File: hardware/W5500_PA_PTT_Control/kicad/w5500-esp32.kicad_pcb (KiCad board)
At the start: 2 copper layers, 115 x 72 mm, 19 parts, among them J1 ESP32_DevKitC_Socket_40P_25.4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, Q1 2SC1815, Q3 2SC1815, Q5 2SJ334, U1 TA48033S, U2 L7805

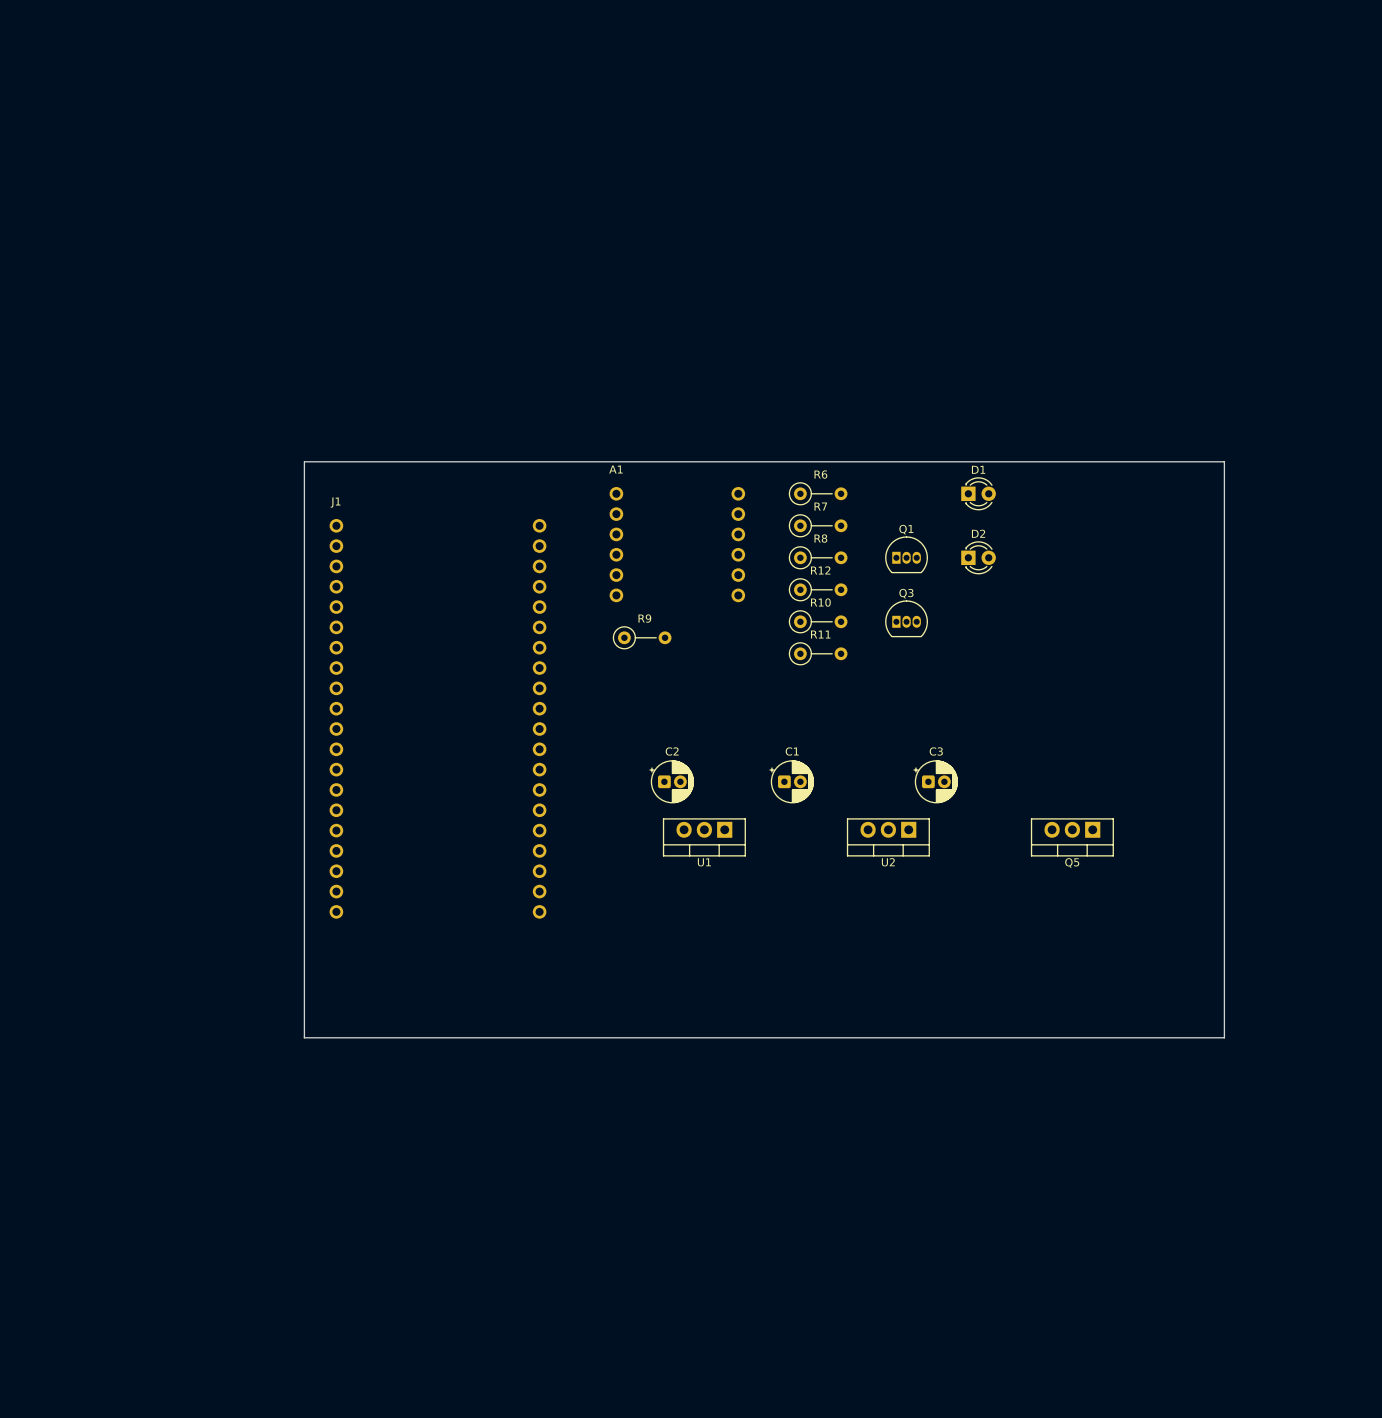
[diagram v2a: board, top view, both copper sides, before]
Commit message: W5500制御基板を縦72×115mmにし、従来基板と同じくW5500を上・ESP32を下に配置
- 外形を横72mm×縦115mm(従来の手配線基板95×72mmを縦に20mm延長)に変更
- 左上にW5500モジュール(RJ45は上端側)、その下にJ1(ESP32 DevKitC、USBは下端側)、
  右側にTO-220(U1・U2・Q5)を縦に23mm間隔で並べ放熱器を右端側に、右下に小物部品とJ2/J5/J6の場所
- W5500モジュール・DevKitC・放熱器・J2/J5/J6の範囲をDwgs.Userに記入(寸法は実物のデータで更新予定)
- DRC違反0件(未配線・J2/J5/J6未指定・既存のGND<NO NET>を除く)。仕様書の配置説明を更新

Co-Authored-By: Claude Opus 5.5 <noreply@anthropic.com>
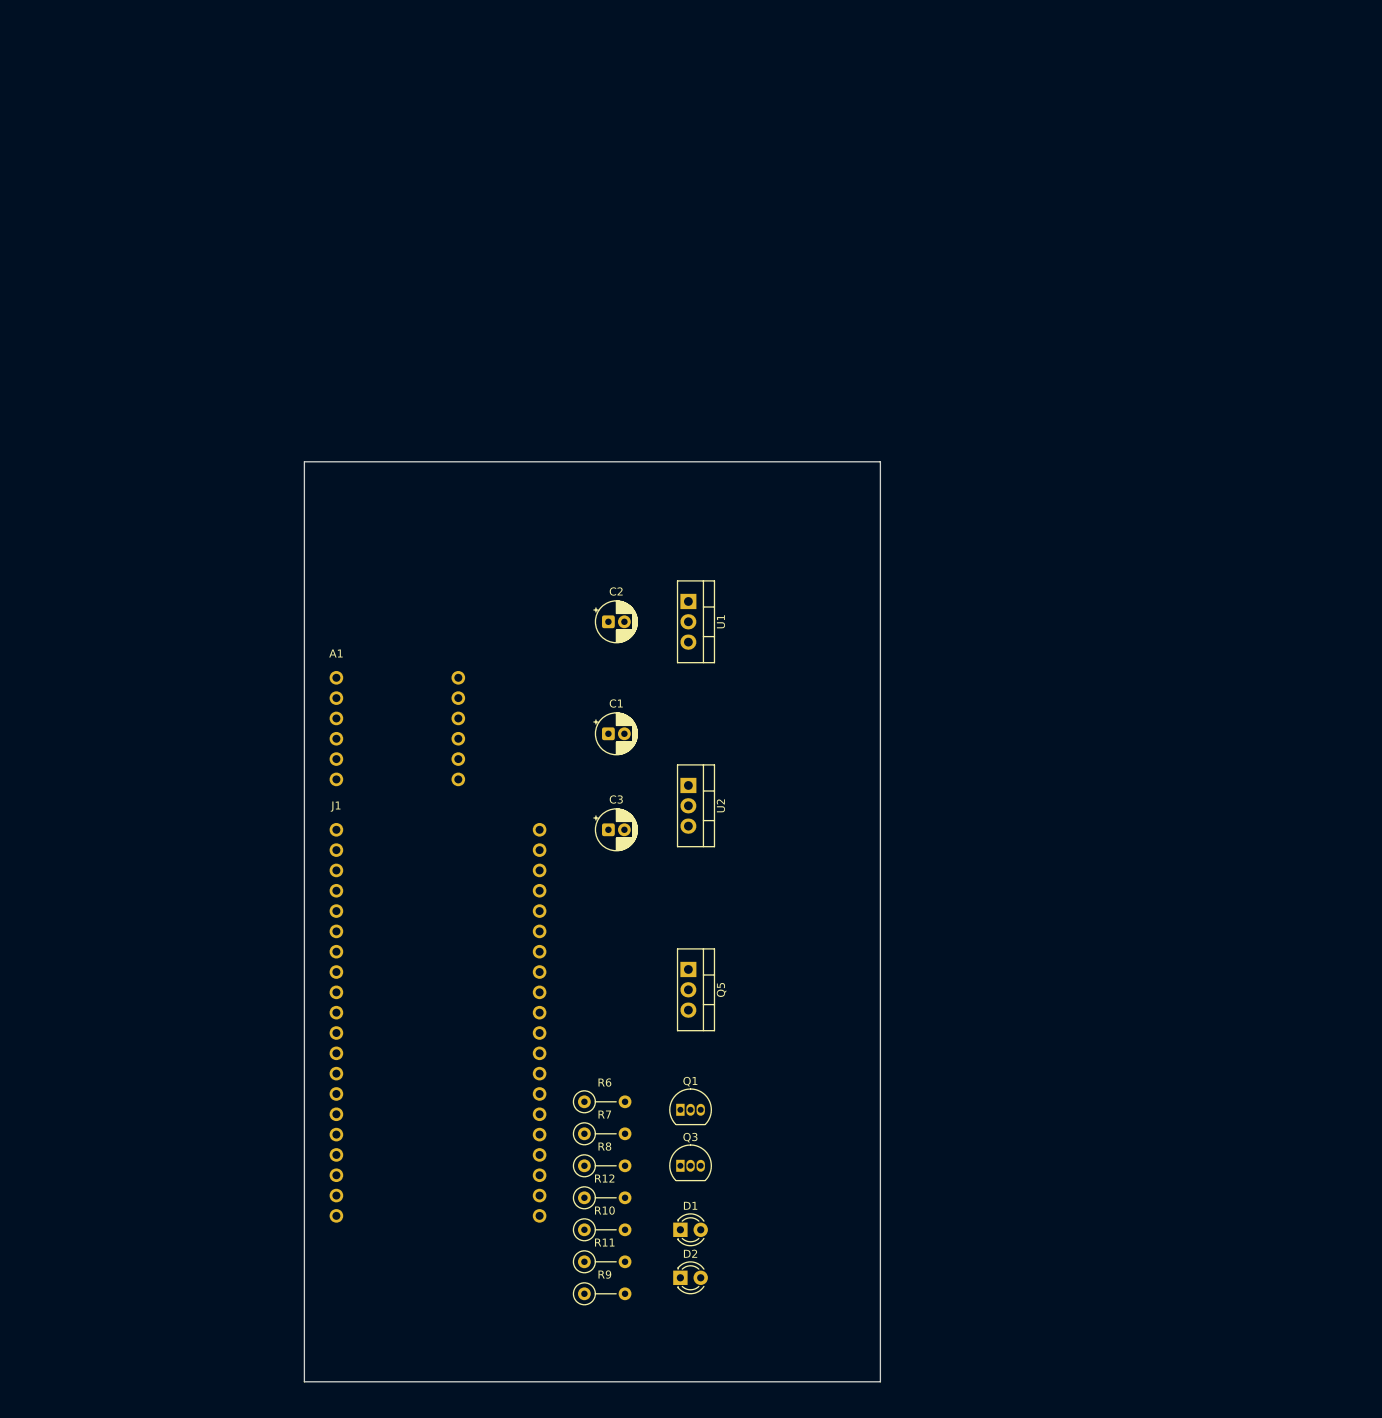
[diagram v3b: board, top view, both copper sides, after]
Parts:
- moved D1 98.8 mm to (147.0, 196.0)
- moved D2 96.9 mm to (147.0, 202.0)
- moved R9 82.2 mm to (135.0, 204.0)
- moved R10 80.7 mm to (135.0, 196.0)
- moved R11 80.7 mm to (135.0, 200.0)
- moved R12 80.7 mm to (135.0, 192.0)
- moved R6 80.7 mm to (135.0, 180.0)
- moved R7 80.7 mm to (135.0, 184.0)
- moved R8 80.7 mm to (135.0, 188.0)
- moved Q1 74.1 mm to (147.0, 181.0)
- moved Q3 73.2 mm to (147.0, 188.0)
- moved Q5 53.5 mm to (148.0, 163.5), turned to 270 degrees
- moved A1 41.9 mm to (104.0, 127.0)
- moved C3 40.4 mm to (138.0, 146.0)
- moved J1 38.0 mm to (104.0, 146.0)
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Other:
- board size 115 x 72 mm -> 72 x 115 mm
- board text added: "20x20"
- board text added: "ESP32 DevKitC(USBは下端側)"
- board text added: "W5500モジュール(RJ45は上端側)"
- board text added: "寸法は実データで更新"
- board text added: "放熱器 Q5"
- board text added: "放熱器 U1"
- board text added: "放熱器 U2"
- board text removed: "放熱器 Q5 20x20"
- board text removed: "放熱器 U1 20x20"
- board text removed: "放熱器 U2 20x20"

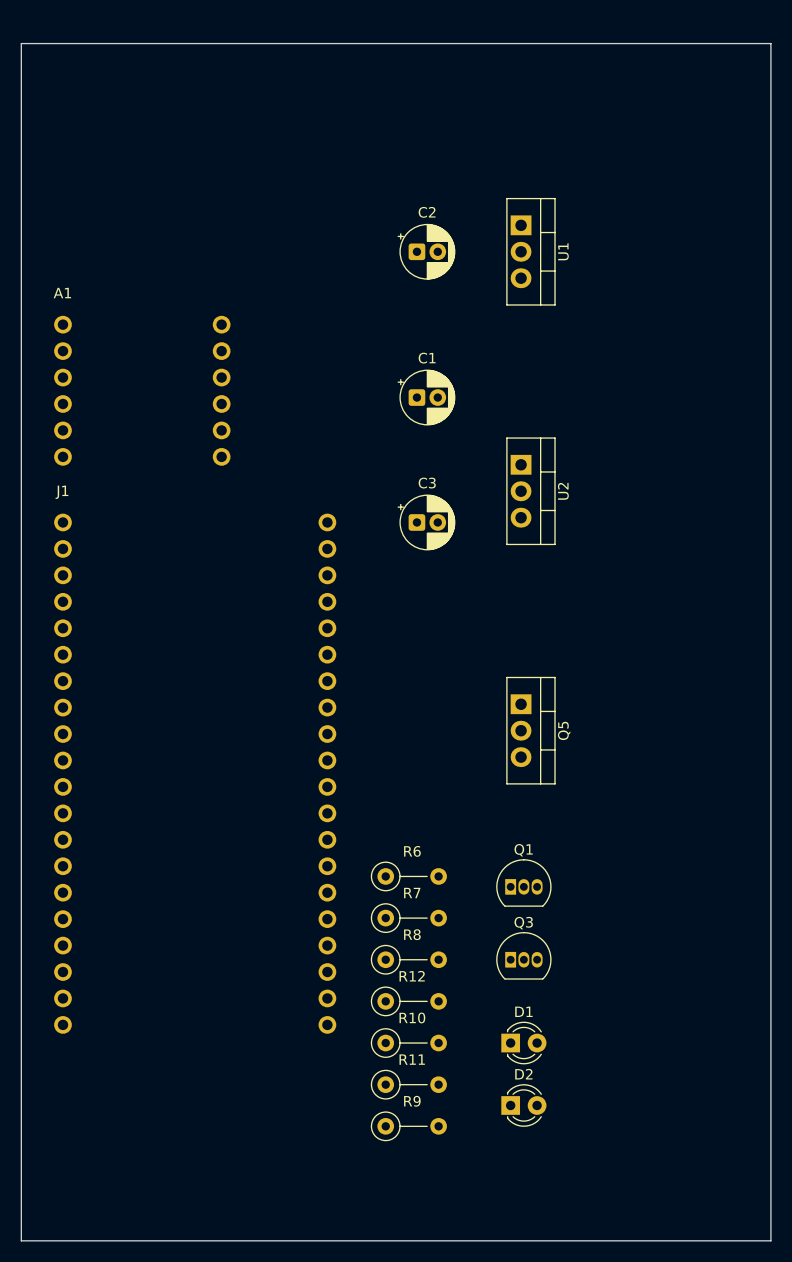
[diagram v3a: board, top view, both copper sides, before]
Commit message: W5500制御基板にM3取付穴を追加し、ケース(LAN_PTT.scad)の開口に合わせて配置
- 取付穴H1〜H4(M3用φ3.2mm、基板専用)をケースのボスと同じ66×109mm間隔(各辺から3mm内側)に追加
- W5500(RJ45)とDevKitC(USB)を前面・背面の開口位置に合わせて左の列へ、抵抗は左端、
  コンデンサはTO-220の間、トランジスタ・LEDは右下へ移動
- ケース内壁・開口部・ボス外径(φ8)・各部品の範囲をDwgs.Userに記入
- DRC違反0件(未配線・J2/J5/J6未指定・既存のGND<NO NET>を除く)。仕様書にケースと取付穴を追記

Co-Authored-By: Claude Opus 5.5 <noreply@anthropic.com>
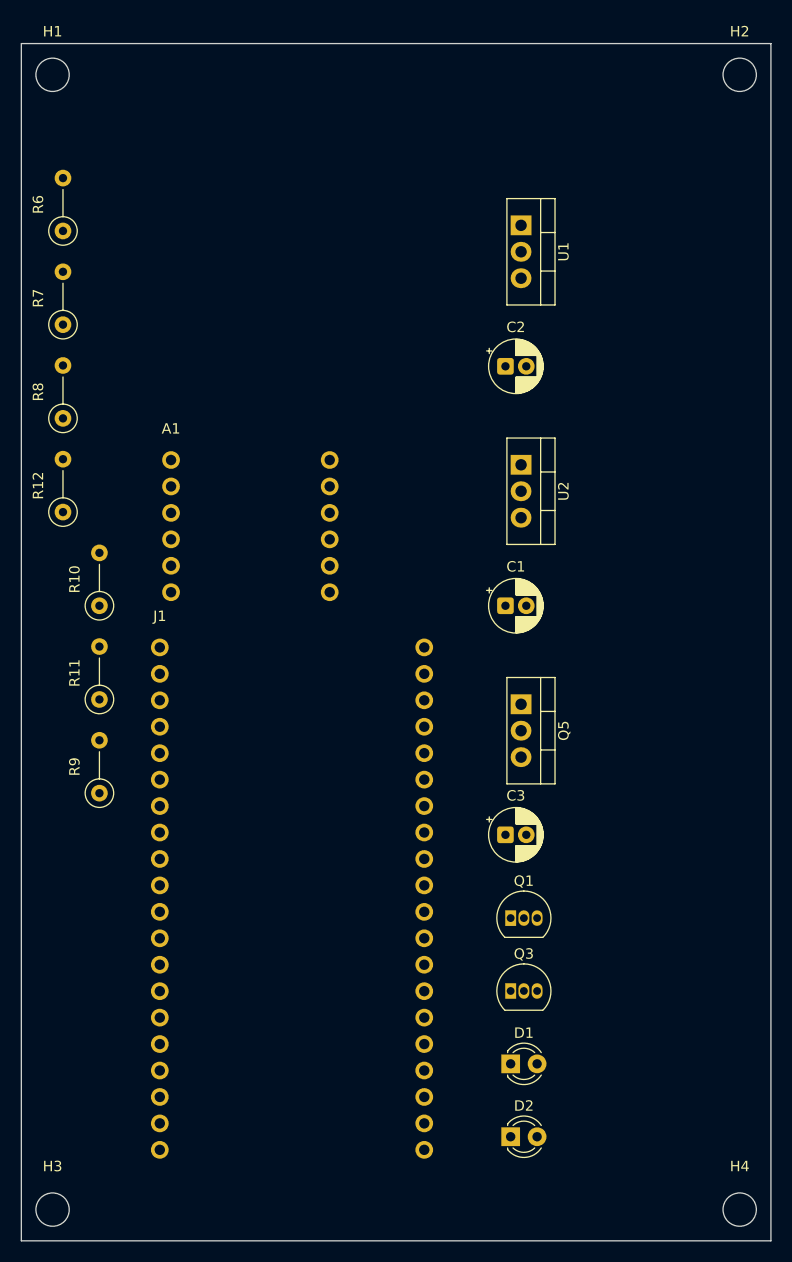
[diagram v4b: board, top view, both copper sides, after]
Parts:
- added H1: MountingHole_3.2mm_M3, MountingHole:MountingHole_3.2mm_M3, F.Cu at (103.0, 103.0)
- added H2: MountingHole_3.2mm_M3, MountingHole:MountingHole_3.2mm_M3, F.Cu at (169.0, 103.0)
- added H3: MountingHole_3.2mm_M3, MountingHole:MountingHole_3.2mm_M3, F.Cu at (103.0, 212.0)
- added H4: MountingHole_3.2mm_M3, MountingHole:MountingHole_3.2mm_M3, F.Cu at (169.0, 212.0)
- moved R6 69.3 mm to (104.0, 118.0), turned to 90 degrees
- moved R7 64.9 mm to (104.0, 127.0), turned to 90 degrees
- moved R8 60.5 mm to (104.0, 136.0), turned to 90 degrees
- moved R12 56.3 mm to (104.0, 145.0), turned to 90 degrees
- moved R10 50.2 mm to (107.5, 154.0), turned to 90 degrees
- moved R11 46.1 mm to (107.5, 163.0), turned to 90 degrees
- moved R9 42.2 mm to (107.5, 172.0), turned to 90 degrees
- moved C3 31.2 mm to (146.5, 176.0)
- moved C1 21.7 mm to (146.5, 154.0)
- moved A1 16.6 mm to (114.4, 140.0)
- moved J1 15.2 mm to (113.3, 158.0)
- moved C2 13.9 mm to (146.5, 131.0)
- moved D2 3.00 mm to (147.0, 205.0)
- moved Q1 3.00 mm to (147.0, 184.0)
- moved Q3 3.00 mm to (147.0, 191.0)
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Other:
- board text added: "ESP32 DevKitC"
- board text added: "W5500モジュール(寸法は実データで更新)"
- board text added: "ケース内壁 80x120"
- board text added: "前面 RJ45開口 x45-63 z10-24"
- board text added: "前面 丸穴 Ø16 z17.5"
- board text added: "放熱器 Q5 20x20"
- board text added: "放熱器 U1 20x20"
- board text added: "放熱器 U2 20x20"
- board text added: "背面 USB開口 15x6 z7"
- board text added: "背面 丸穴 Ø16 z17.5"
- board text removed: "20x20"
- board text removed: "ESP32 DevKitC(USBは下端側)"
- board text removed: "W5500モジュール(RJ45は上端側)"
- board text removed: "寸法は実データで更新"
- board text removed: "放熱器 Q5"
- board text removed: "放熱器 U1"
- board text removed: "放熱器 U2"

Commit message: W5500とDevKitCのフットプリントを実物の資料に合わせて修正し、ケースの開口に合わせて配置
- A1(W5500 Lite): USR-ES1データシートに合わせ、ピン列間隔を15.24→20.32mm、7〜12番をRJ45側から数える順に修正
  (従来は右列の信号が逆につながる配置だった)。新フットプリントW5500_Lite_USR-ES1_2x06_P2.54mm_20.32mm
- J1(DevKitCソケット): Freenove公式ピン配置図に合わせ、ピンの並びを上下反転(1番5V・21番GNDがUSB-C側)。
  従来は鏡像の並びで、5Vが3V3/GNDのピンにつながる配置だった
- RJ45をケース前面の角穴(基板x=122)、USB-Cを背面の角丸穴(x=126)に合わせて配置
- 接続一覧(日英・Word・PDF)に修正内容を追記、回路図PDF/SVGを再出力。DRC違反0件

Co-Authored-By: Claude Opus 5.5 <noreply@anthropic.com>
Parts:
- A1: footprint project_footprints:W5500_Lite_2x06_P2.54mm_15.24mm -> project_footprints:W5500_Lite_USR-ES1_2x06_P2.54mm_20.32mm
- moved A1 33.2 mm to (111.8, 106.9)
- moved J1 7.24 mm to (113.3, 165.2)
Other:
- board text added: "Freenove ESP32 WROOM 約27x58.5(要実測)"
- board text added: "W5500 Lite (USR-ES1) 23x25"
- board text added: "背面 USB-C開口 15x6 z7"
- board text removed: "ESP32 DevKitC"
- board text removed: "W5500モジュール(寸法は実データで更新)"
- board text removed: "背面 USB開口 15x6 z7"

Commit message: J2(+12V入力)・J5(12V出力)・J6(PTT出力)を電線はんだ付け用パッドとして配置
- ケースの丸型コネクタ(WTN-11-1253 8P)へ電線でつなぐ前提で、回路図にフットプリントを指定
  (J2・J5: Connector_Wire SolderWire-1sqmm、J6: SolderWire-0.5sqmm)
- J2は前面の丸型コネクタ側(右上)、J5・J6は背面の丸型コネクタ側(右下)に配置
- 「フットプリントが見つからない」3件を解消。DRC違反0件、ERCは変更前と同じ15件
- 仕様書(日英・Word・PDF)の配置説明を更新、回路図PDF/SVGを再出力

Co-Authored-By: Claude Opus 5.5 <noreply@anthropic.com>
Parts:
- added J2: DC_IN_13V8, Connector_Wire:SolderWire-1sqmm_1x02_P5.4mm_D1.4mm_OD2.7mm, F.Cu at (150.0, 106.0)
- added J5: Power, Connector_Wire:SolderWire-1sqmm_1x02_P5.4mm_D1.4mm_OD2.7mm, F.Cu at (157.0, 188.0)
- added J6: PTT_ON, Connector_Wire:SolderWire-0.5sqmm_1x02_P4.6mm_D0.9mm_OD2.1mm, F.Cu at (157.0, 197.0)
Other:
- board text removed: "J2/J5/J6"

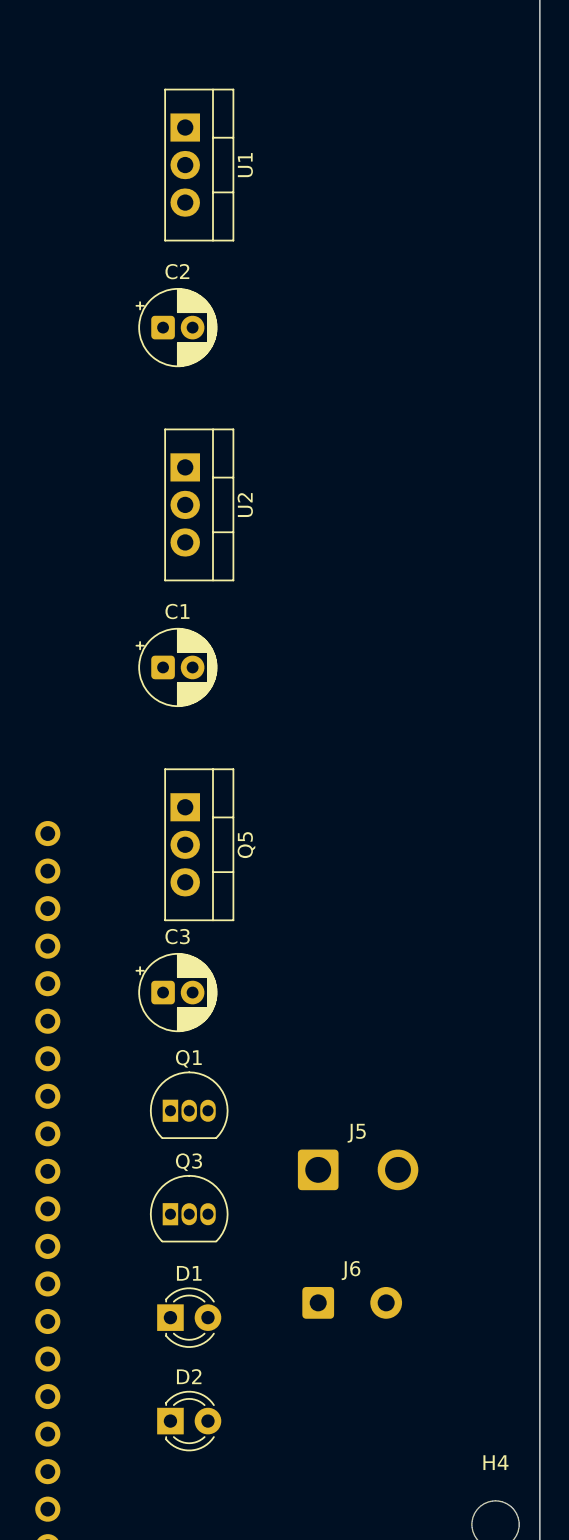
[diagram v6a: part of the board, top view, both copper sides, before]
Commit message: W5500制御基板: 丸型コネクタ裏に配線用の空き20mmを確保し4層化
- 放熱器の列を22mm間隔にして下へ移動、Q1/Q3/D1/D2/J5/J6を背面側の空きの手前へ移動
- 前面・背面の丸型コネクタ裏の空き範囲をDwgs.Userに記入
- 4層基板に変更(In1=GND、In2=電源、層設定のみ)
- 仕様書(日英)をRev.2.5に更新、Word/PDFを再生成

Co-Authored-By: Claude Opus 5.5 <noreply@anthropic.com>
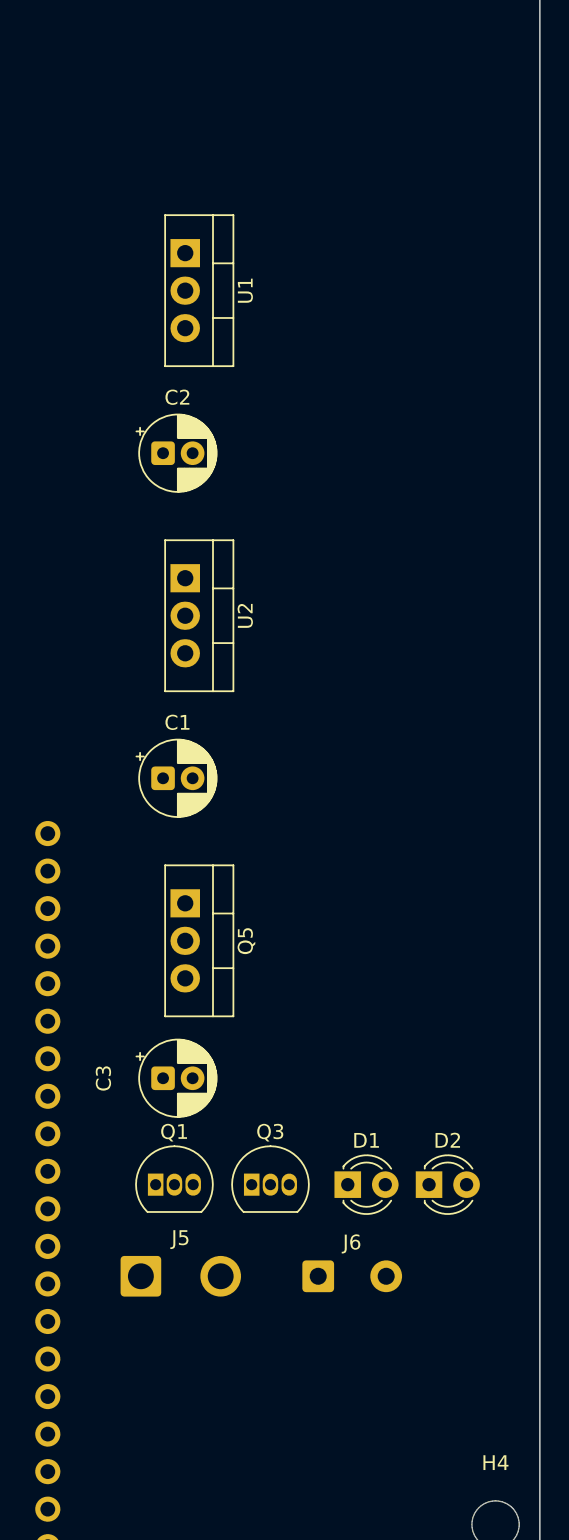
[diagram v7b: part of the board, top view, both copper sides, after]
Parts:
- moved D2 23.7 mm to (164.5, 189.0)
- moved D1 15.0 mm to (159.0, 189.0)
- moved J5 14.0 mm to (145.0, 195.2)
- moved C2 8.50 mm to (146.5, 139.5)
- moved U1 8.50 mm to (148.0, 126.0)
- moved C1 7.50 mm to (146.5, 161.5)
- moved U2 7.50 mm to (148.0, 148.0)
- moved Q5 6.50 mm to (148.0, 170.0)
- moved Q3 5.85 mm to (152.5, 189.0)
- moved C3 5.80 mm to (146.5, 181.8)
- moved Q1 5.10 mm to (146.0, 189.0)
- moved J6 1.80 mm to (157.0, 195.2)
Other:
- copper layers 2 -> 4
- board text added: "前面コネクタ裏 空き 20mm(配線用)"
- board text added: "背面コネクタ裏 空き 20mm(配線用)"
